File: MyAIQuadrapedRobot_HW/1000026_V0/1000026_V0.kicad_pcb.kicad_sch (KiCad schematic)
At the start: 27 parts, among them J1 533750410, J2 0525591853, J3 532580229, J5 532580229, J9 0525591853, SW1 TL3305CF260QG, U1 TXB0108PWR, U2 MAX7480ESA+

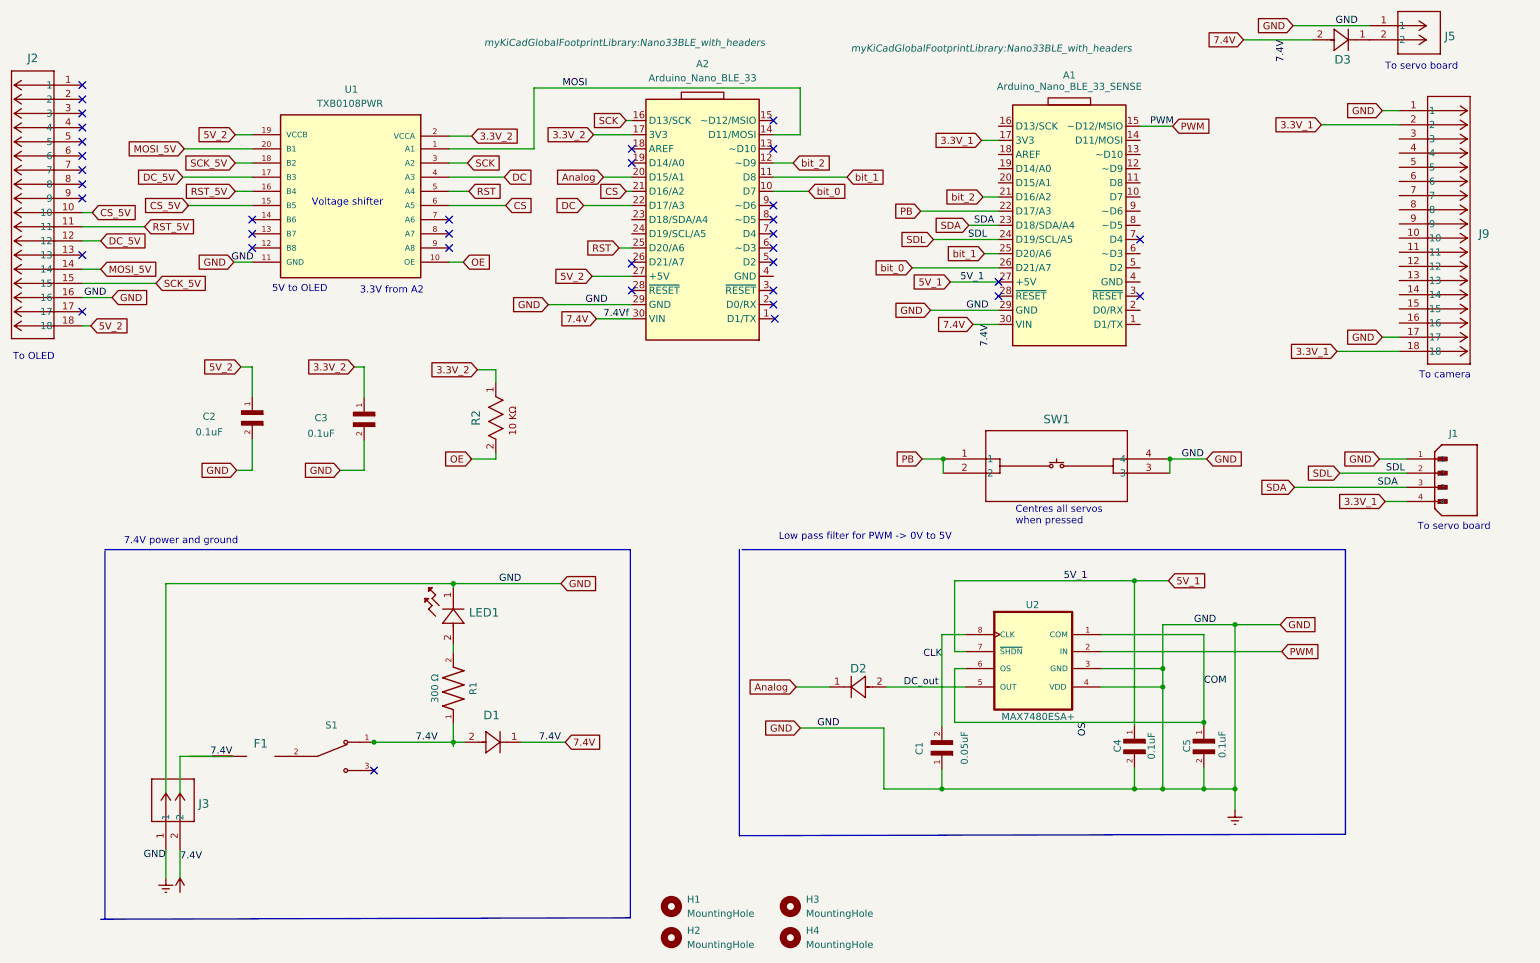
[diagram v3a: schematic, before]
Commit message: All tracks in place but needs improvement.
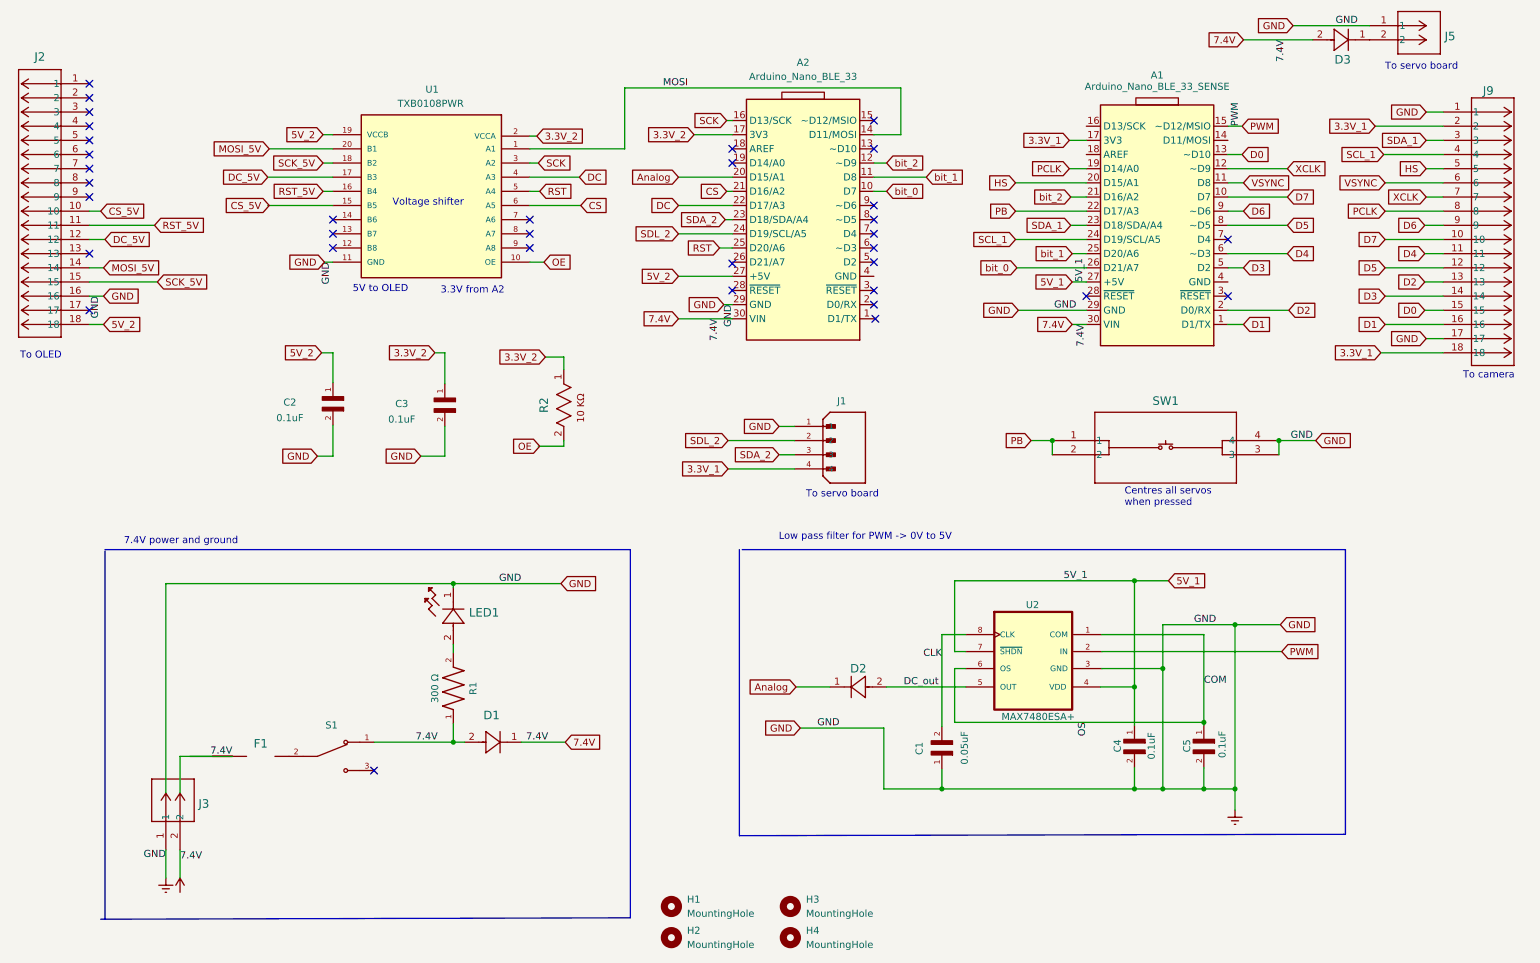
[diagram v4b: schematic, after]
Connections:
- net 5V_1: now also U2.4 (VDD)
- net GNDREF: no longer U2.4 (VDD)
- net D1: now reaches A1.1 (D1/TX)
- net D1: now also J9.16
- net D7: now reaches A1.10 (D7)
- net D7: now also J9.10
- net VSYNC: now reaches A1.11 (D8)
- net VSYNC: now also J9.6
- net XCLK: now reaches A1.12 (~D9)
- net XCLK: now also J9.7
- net D0: now reaches A1.13 (~D10)
- net D0: now also J9.15
- net PCLK: now reaches A1.19 (D14/A0)
- net PCLK: now also J9.8
- net D2: now reaches A1.2 (D0/RX)
- net D2: now also J9.13
- net HS: now reaches A1.20 (D15/A1)
- net HS: now also J9.5
- net D3: now reaches A1.5 (D2)
- net D3: now also J9.14
- net D4: now reaches A1.6 (~D3)
- net D4: now also J9.11
- net D5: now reaches A1.8 (~D5)
- net D5: now also J9.12
- net D6: now reaches A1.9 (~D6)
- net D6: now also J9.9
- net SDA_1: now reaches J9.3
- net SDA_1: now also A1.23 (D18/SDA/A4)
- net SCL_1: now reaches J9.4
- net SCL_1: now also A1.24 (D19/SCL/A5)
- net SDA_2: now reaches A2.23 (D18/SDA/A4)
- net SDA_2: now also J1.3
- net SDL_2: now reaches A2.24 (D19/SCL/A5)
- net SDL_2: now also J1.2
- removed net SDA: A1.23 (D18/SDA/A4), J1.3
- removed net SDL: A1.24 (D19/SCL/A5), J1.2
- no-connect marks 36 -> 35
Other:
- moved on the sheet: A1, A2, C2, C3, J1, J2, J9, R2, SW1, U1

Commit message: Revisions in progress for change in sizes of some SMD components.
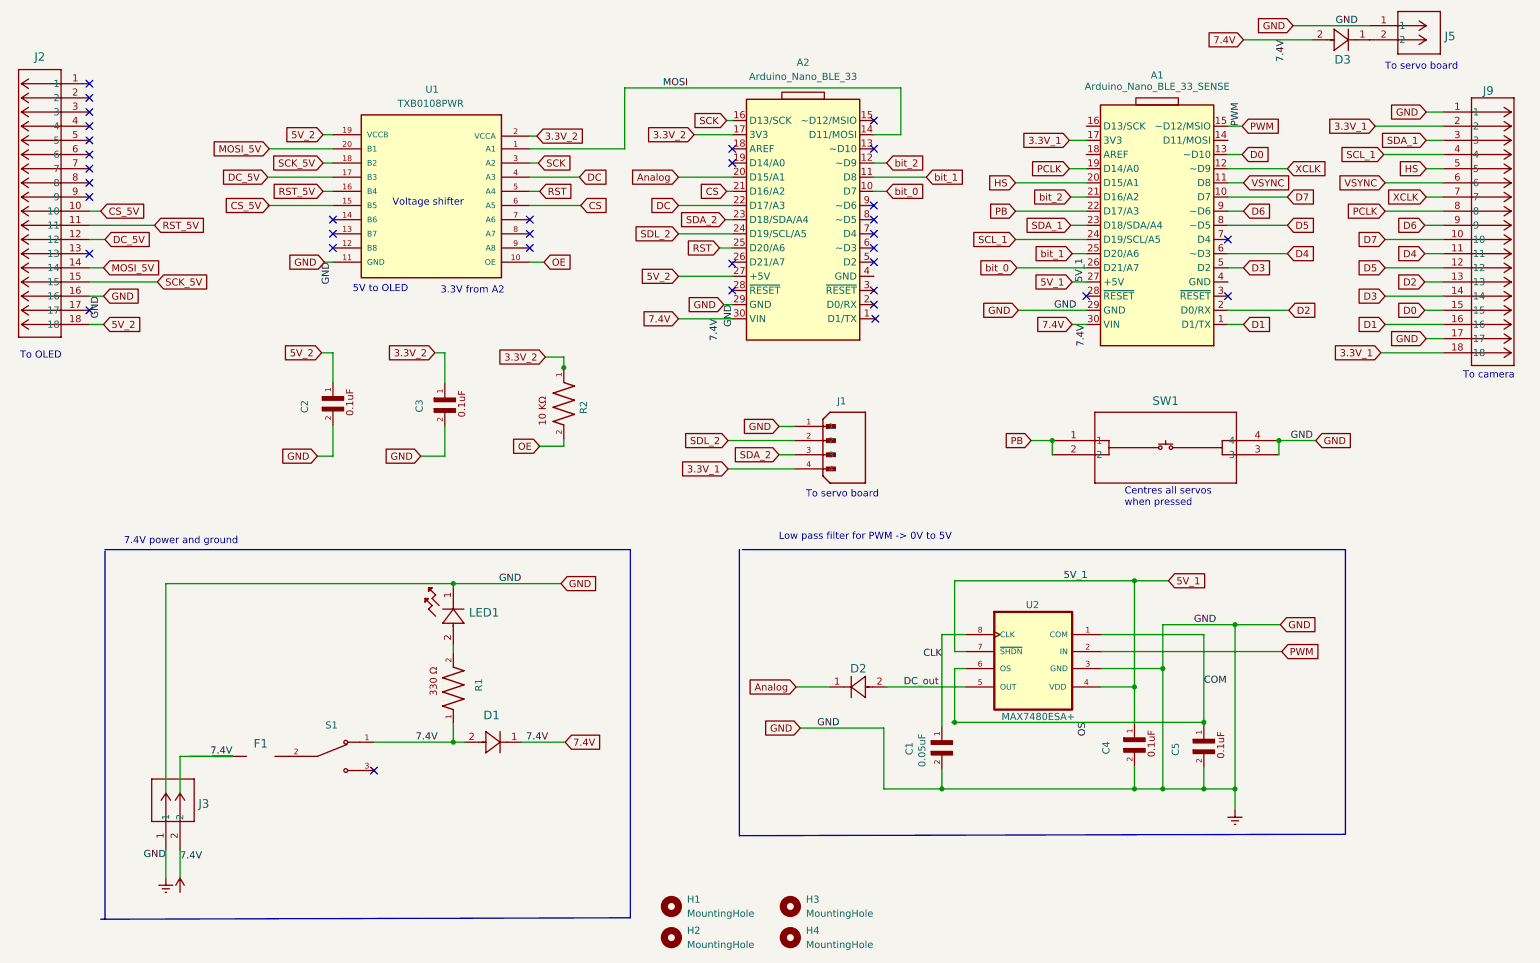
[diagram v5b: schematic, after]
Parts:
- removed C2, C3, C4, C5: CL05A104KA5NNNC, myKiCadGlobalFootprintLibrary:CAPC1005X55N, symbol myKiCadGlobalSymbolLibrary:CL05A104KA5NNNC
- removed R1: RMCF2512FT330R, myKiCadGlobalFootprintLibrary:RESC6332X70N, symbol myKiCadGlobalSymbolLibrary:RMCF2512FT330R
- removed R2: RC0402JR-0710KL, myKiCadGlobalFootprintLibrary:RC0402JR-0710KL, symbol myKiCadGlobalSymbolLibrary:RC0402JR-0710KL
- added C2, C3, C4, C5: 12102C104KAT2A, myKiCadGlobalFootprintLibrary:12102C104KAT2A, symbol myKiCadGlobalSymbolLibrary:12102C104KAT2A
- added R1: RMCF1210JT330R, myKiCadGlobalFootprintLibrary:RMCF1210JT330R, symbol myKiCadGlobalSymbolLibrary:RMCF1210JT330R
- added R2: RMCF1210JT10K0, myKiCadGlobalFootprintLibrary:RMCF1210JT10K0, symbol myKiCadGlobalSymbolLibrary:RMCF1210JT10K0
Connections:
- net 3.3V_2: now also C3.1, R2.1
- net 5V_1: now also C4.1
- net 5V_2: now also C2.1
- net 7.4V: now also R1.1
- net CLK: now also C1.1; no longer C1.2
- net COM: now also C5.1
- net GNDREF: now also C1.2, C2.2, C3.2, C4.2, C5.2; no longer C1.1
- net OE: now also R2.2
- net at LED1.2: now also R1.2

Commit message: Minor revisions.
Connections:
- no-connect marks 35 -> 40
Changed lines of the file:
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@@
   (no_connect (at 27.432 31.75))
   (no_connect (at 27.432 69.85))
+  (no_connect (at 206.248 36.83))
   (no_connect (at 142.748 40.894))
   (no_connect (at 27.432 29.21))
   (no_connect (at 142.748 66.294))
+  (no_connect (at 168.148 63.754))
   (no_connect (at 168.148 40.894))
   (no_connect (at 27.432 39.37))
@@
   (no_connect (at 106.426 58.674))
   (no_connect (at 106.426 56.134))
+  (no_connect (at 231.648 39.37))
+  (no_connect (at 206.248 41.91))
   (no_connect (at 168.148 56.134))
+  (no_connect (at 231.648 64.77))
   (no_connect (at 142.748 61.468))
   (no_connect (at 168.148 51.054))

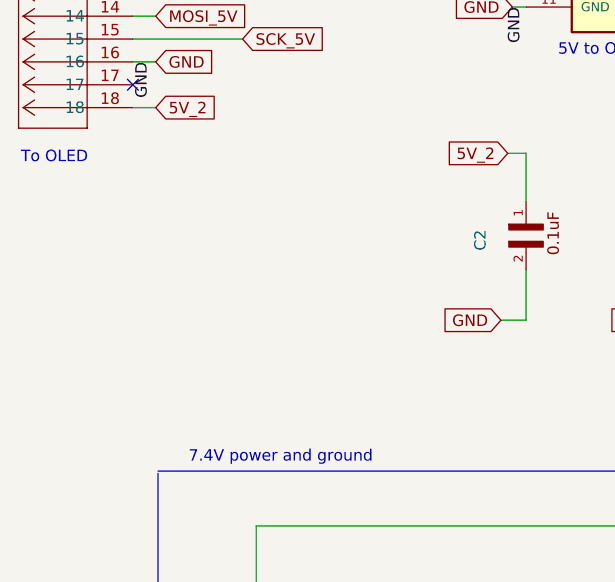
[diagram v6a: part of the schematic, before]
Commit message: Added components for 5V regulator.
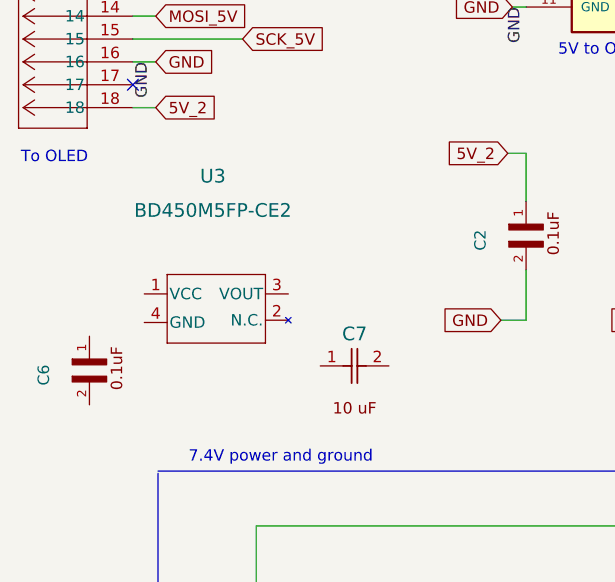
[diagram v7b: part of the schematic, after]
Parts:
- added C6: 12102C104KAT2A, myKiCadGlobalFootprintLibrary:12102C104KAT2A, symbol myKiCadGlobalSymbolLibrary:12102C104KAT2A
- added C7: CL32A106KAULNNE, myKiCadGlobalFootprintLibrary:CL32A106KAULNNE, symbol myKiCadGlobalSymbolLibrary:CL32A106KAULNNE
- added U3: BD450M5FP-CE2, myKiCadGlobalFootprintLibrary:BD450M5FP-CE2, symbol myKiCadGlobalSymbolLibrary:BD450M5FP-CE2
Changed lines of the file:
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@@
+    (pin "2")
+  )
+  (symbol (lib_id "myKiCadGlobalSymbolLibrary:CL32A106KAULNNE") (at 48.26 101.092 0) (unit 1)
+    (in_bom yes) (on_board yes) (fields_autoplaced)
+    (property "Reference" "C7" (id 0) (at 52.07 97.536 0)
+      (effects (font (size 1.524 1.524)))
+    )
+    (property "Value" "CL32A106KAULNNE" (id 1) (at 52.07 97.536 0)
+      (effects (font (size 1.524 1.524)) hide)
+    )
+    (property "Footprint" "myKiCadGlobalFootprintLibrary:CL32A106KAULNNE" (id 2) (at 52.07 97.028 0)
+      (effects (font (size 1.27 1.27) italic) hide)
+    )
+    (property "Datasheet" "CL32A106KAULNNE" (id 3) (at 50.8 116.967 0)
+      (effects (font (size 1.27 1.27) italic) hide)
+    )
+    (pin "1")
     (pin "2")
   )
@@
     (pin "9")
   )
+  (symbol (lib_id "myKiCadGlobalSymbolLibrary:BD450M5FP-CE2") (at 16.002 90.932 0) (unit 1)
+    (in_bom yes) (on_board yes) (fields_autoplaced)
+    (property "Reference" "U3" (id 0) (at 36.322 80.01 0)
+      (effects (font (size 1.524 1.524)))
+    )
+    (property "Value" "BD450M5FP-CE2" (id 1) (at 36.322 83.82 0)
+      (effects (font (size 1.524 1.524)))
+    )
+    (property "Footprint" "myKiCadGlobalFootprintLibrary:BD450M5FP-CE2" (id 2) (at 33.02 113.538 0)
+      (effects (font (size 1.27 1.27) italic) hide)
+    )
+    (property "Datasheet" "BD450M5FP-CE2" (id 3) (at 33.782 116.332 0)
+      (effects (font (size 1.27 1.27) italic) hide)
+    )
+    (pin "1")
+    (pin "2")
+    (pin "3")
+    (pin "4")
+  )
   (symbol (lib_id "myKiCadGlobalSymbolLibrary:1N4148WX-TP") (at 170.434 137.414 0) (mirror y) (unit 1)
     (in_bom yes) (on_board yes) (fields_autoplaced)
@@
     (pin "4")
   )
-  (symbol (lib_name "12102C104KAT2A_2") (lib_id "myKiCadGlobalSymbolLibrary:12102C104KAT2A") (at 214.884 146.558 270) (unit 1)
+  (symbol (lib_id "myKiCadGlobalSymbolLibrary:12102C104KAT2A") (at 214.884 146.558 270) (unit 1)
     (in_bom yes) (on_board yes)
     (property "Reference" "C4" (id 0) (at 209.804 148.336 0))
@@
     (pin "9")
   )
-  (symbol (lib_name "12102C104KAT2A_1") (lib_id "myKiCadGlobalSymbolLibrary:12102C104KAT2A") (at 227.33 146.812 270) (unit 1)
+  (symbol (lib_id "myKiCadGlobalSymbolLibrary:12102C104KAT2A") (at 227.33 146.812 270) (unit 1)
     (in_bom yes) (on_board yes)
     (property "Reference" "C5" (id 0) (at 222.25 148.59 0))
@@
     (pin "2")
   )
-  (symbol (lib_name "12102C104KAT2A_2") (lib_id "myKiCadGlobalSymbolLibrary:12102C104KAT2A") (at 71.12 85.344 270) (unit 1)
+  (symbol (lib_id "myKiCadGlobalSymbolLibrary:12102C104KAT2A") (at 71.12 85.344 270) (unit 1)
     (in_bom yes) (on_board yes)
     (property "Reference" "C2" (id 0) (at 66.04 87.122 0))
@@
     )
     (property "Datasheet" "" (id 3) (at 71.12 85.344 0)
+      (effects (font (size 1.27 1.27)) hide)
+    )
+    (pin "1")
+    (pin "2")
+  )
+  (symbol (lib_id "myKiCadGlobalSymbolLibrary:12102C104KAT2A") (at 22.606 100.33 270) (unit 1)
+    (in_bom yes) (on_board yes)
+    (property "Reference" "C6" (id 0) (at 17.526 102.108 0))
+    (property "Value" "12102C104KAT2A" (id 1) (at 20.32 89.154 0)
+      (effects (font (size 1.27 1.27)) hide)
+    )
+    (property "Footprint" "myKiCadGlobalFootprintLibrary:12102C104KAT2A" (id 2) (at 27.686 101.6 0)
+      (effects (font (size 1.27 1.27)) hide)
+    )
+    (property "Datasheet" "" (id 3) (at 22.606 100.33 0)
       (effects (font (size 1.27 1.27)) hide)
     )
@@
       (reference "C5") (unit 1) (value "12102C104KAT2A") (footprint "myKiCadGlobalFootprintLibrary:12102C104KAT2A")
     )
+    (path "/a7977b60-e106-49e6-b80d-8d42e0531c95"
+      (reference "C6") (unit 1) (value "12102C104KAT2A") (footprint "myKiCadGlobalFootprintLibrary:12102C104KAT2A")
+    )
+    (path "/0709eb23-0877-477f-8066-4d8944855ad3"
+      (reference "C7") (unit 1) (value "CL32A106KAULNNE") (footprint "myKiCadGlobalFootprintLibrary:CL32A106KAULNNE")
+    )
     (path "/29a083e9-34e8-4c5e-bbe7-f07292034634"
       (reference "D1") (unit 1) (value "1N4148WX-TP") (footprint "myKiCadGlobalFootprintLibrary:1N4148WT")
@@
       (reference "U2") (unit 1) (value "MAX7480ESA+") (footprint "myKiCadGlobalFootprintLibrary:MAX7480ESA")
     )
-  )
+    (path "/1c24028c-59e1-471f-9d33-4d1d6cab5304"
+      (reference "U3") (unit 1) (value "BD450M5FP-CE2") (footprint "myKiCadGlobalFootprintLibrary:BD450M5FP-CE2")
+    )
+  )
